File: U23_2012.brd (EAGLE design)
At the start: 150 x 100 mm, 68 parts, among them T1 BC337, X2 J1006F01P

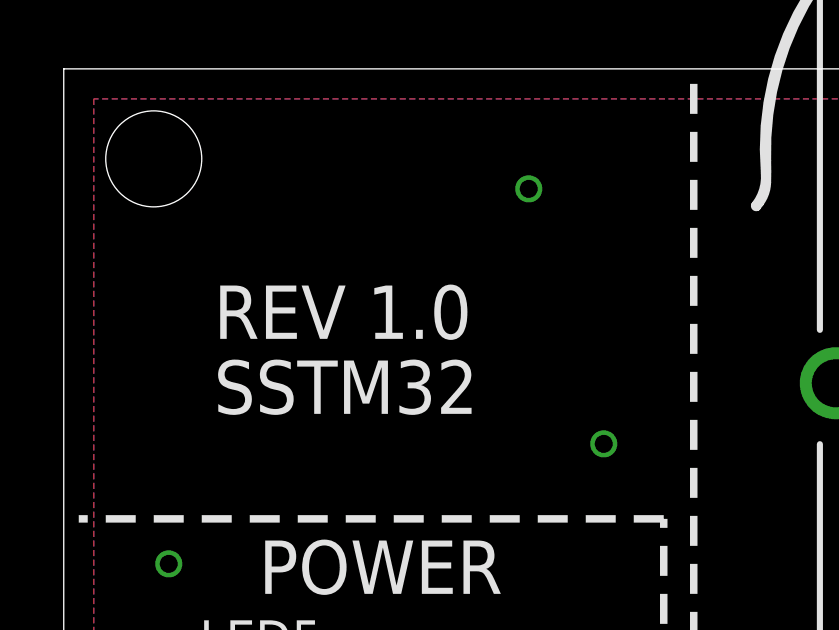
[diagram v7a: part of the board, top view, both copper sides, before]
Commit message: fixes not connected vias. rev_1.1
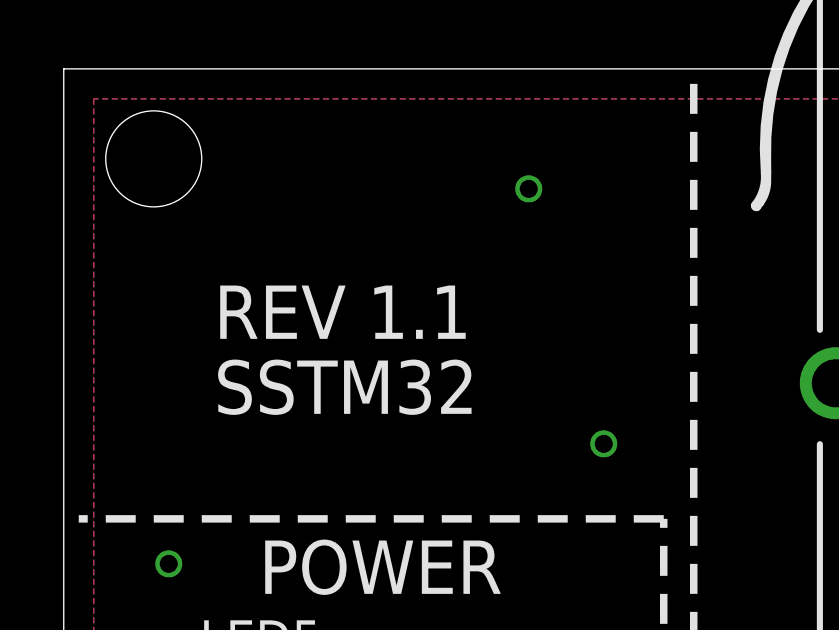
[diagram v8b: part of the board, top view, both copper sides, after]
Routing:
- net GND: vias 5 -> 45
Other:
- board text added: "REV 1.1"
- board text removed: "REV 1.0"
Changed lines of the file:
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@@
 <text x="30.5" y="20.5" size="3.81" layer="25">CHAOS COMPUTER CLUB COLOGNE</text>
 <text x="73.5" y="36.5" size="1.778" layer="25">R2R DAC</text>
-<text x="5" y="91" size="1.778" layer="25">REV 1.0</text>
+<text x="5" y="91" size="1.778" layer="25">REV 1.1</text>
 <text x="5" y="88.5" size="1.778" layer="25">SSTM32</text>
 <polygon width="0" layer="21">
@@
 <via x="6" y="40" extent="1-16" drill="0.6" shape="square"/>
 <via x="71" y="80.5" extent="1-16" drill="0.6" shape="square"/>
+<via x="15.5" y="96" extent="1-16" drill="0.6" shape="square"/>
+<via x="18" y="87.5" extent="1-16" drill="0.6" shape="square"/>
+<via x="3.5" y="83.5" extent="1-16" drill="0.6" shape="square"/>
+<via x="9" y="64" extent="1-16" drill="0.6" shape="square"/>
+<via x="9" y="56.5" extent="1-16" drill="0.6" shape="square"/>
+<via x="11" y="12.5" extent="1-16" drill="0.6" shape="square"/>
+<via x="25.5" y="16.5" extent="1-16" drill="0.6" shape="square"/>
+<via x="24" y="24" extent="1-16" drill="0.6" shape="square"/>
+<via x="31.5" y="27" extent="1-16" drill="0.6" shape="square"/>
+<via x="39.5" y="14.5" extent="1-16" drill="0.6" shape="square"/>
+<via x="49.5" y="13.5" extent="1-16" drill="0.6" shape="square"/>
+<via x="44.5" y="14.5" extent="1-16" drill="0.6" shape="square"/>
+<via x="51" y="19.5" extent="1-16" drill="0.6" shape="square"/>
+<via x="57" y="22.5" extent="1-16" drill="0.6" shape="square"/>
+<via x="31" y="31.5" extent="1-16" drill="0.6" shape="square"/>
+<via x="44.5" y="31" extent="1-16" drill="0.6" shape="square"/>
+<via x="48" y="31" extent="1-16" drill="0.6" shape="square"/>
+<via x="56.5" y="31.5" extent="1-16" drill="0.6" shape="square"/>
+<via x="56.5" y="44.5" extent="1-16" drill="0.6" shape="square"/>
+<via x="50" y="45" extent="1-16" drill="0.6" shape="square"/>
+<via x="50" y="49.5" extent="1-16" drill="0.6" shape="square"/>
+<via x="56" y="51" extent="1-16" drill="0.6" shape="square"/>
+<via x="66" y="58.5" extent="1-16" drill="0.6" shape="square"/>
+<via x="35.5" y="90" extent="1-16" drill="0.6" shape="square"/>
+<via x="71.5" y="87" extent="1-16" drill="0.6" shape="square"/>
+<via x="76.5" y="83" extent="1-16" drill="0.6" shape="square"/>
+<via x="92" y="77" extent="1-16" drill="0.6" shape="square"/>
+<via x="115.5" y="77" extent="1-16" drill="0.6" shape="square"/>
+<via x="129.5" y="77" extent="1-16" drill="0.6" shape="square"/>
+<via x="146" y="77.5" extent="1-16" drill="0.6" shape="square"/>
+<via x="118" y="58" extent="1-16" drill="0.6" shape="square"/>
+<via x="99.5" y="58" extent="1-16" drill="0.6" shape="square"/>
+<via x="97.5" y="44.5" extent="1-16" drill="0.6" shape="square"/>
+<via x="129.5" y="35" extent="1-16" drill="0.6" shape="square"/>
+<via x="123.5" y="28.5" extent="1-16" drill="0.6" shape="square"/>
+<via x="145.5" y="26.5" extent="1-16" drill="0.6" shape="square"/>
+<via x="146" y="11" extent="1-16" drill="0.6" shape="square"/>
+<via x="123" y="3.5" extent="1-16" drill="0.6" shape="square"/>
+<via x="86" y="5.5" extent="1-16" drill="0.6" shape="square"/>
+<via x="71.5" y="3.5" extent="1-16" drill="0.6" shape="square"/>
+<wire x1="64.5" y1="3" x2="71.5" y2="3.5" width="0" layer="19" extent="1-1"/>
 </signal>
 <signal name="PE15">
@@
 </polygon>
 </signal>
-<signal name="N$22">
-<via x="92" y="77" extent="1-16" drill="0.6" shape="square"/>
-</signal>
-<signal name="N$25">
-<via x="115.5" y="77" extent="1-16" drill="0.6" shape="square"/>
-</signal>
-<signal name="N$26">
-<via x="129.5" y="77" extent="1-16" drill="0.6" shape="square"/>
-</signal>
-<signal name="N$27">
-<via x="146" y="77.5" extent="1-16" drill="0.6" shape="square"/>
-</signal>
-<signal name="N$28">
-<via x="146" y="11" extent="1-16" drill="0.6" shape="square"/>
-</signal>
-<signal name="N$29">
-<via x="145.5" y="26.5" extent="1-16" drill="0.6" shape="square"/>
-</signal>
-<signal name="N$30">
-<via x="129.5" y="35" extent="1-16" drill="0.6" shape="square"/>
-</signal>
-<signal name="N$31">
-<via x="123.5" y="28.5" extent="1-16" drill="0.6" shape="square"/>
-</signal>
-<signal name="N$32">
-<via x="97.5" y="44.5" extent="1-16" drill="0.6" shape="square"/>
-</signal>
-<signal name="N$33">
-<via x="66" y="58.5" extent="1-16" drill="0.6" shape="square"/>
-</signal>
-<signal name="N$34">
-<via x="99.5" y="58" extent="1-16" drill="0.6" shape="square"/>
-</signal>
-<signal name="N$35">
-<via x="118" y="58" extent="1-16" drill="0.6" shape="square"/>
-</signal>
-<signal name="N$36">
-<via x="56" y="51" extent="1-16" drill="0.6" shape="square"/>
-</signal>
-<signal name="N$37">
-<via x="50" y="49.5" extent="1-16" drill="0.6" shape="square"/>
-</signal>
-<signal name="N$38">
-<via x="50" y="45" extent="1-16" drill="0.6" shape="square"/>
-</signal>
-<signal name="N$39">
-<via x="56.5" y="44.5" extent="1-16" drill="0.6" shape="square"/>
-</signal>
-<signal name="N$40">
-<via x="56.5" y="31.5" extent="1-16" drill="0.6" shape="square"/>
-</signal>
-<signal name="N$41">
-<via x="48" y="31" extent="1-16" drill="0.6" shape="square"/>
-</signal>
-<signal name="N$42">
-<via x="44.5" y="31" extent="1-16" drill="0.6" shape="square"/>
-</signal>
-<signal name="N$43">
-<via x="51" y="19.5" extent="1-16" drill="0.6" shape="square"/>
-</signal>
-<signal name="N$44">
-<via x="57" y="22.5" extent="1-16" drill="0.6" shape="square"/>
-</signal>
-<signal name="N$45">
-<via x="49.5" y="13.5" extent="1-16" drill="0.6" shape="square"/>
-</signal>
-<signal name="N$46">
-<via x="44.5" y="14.5" extent="1-16" drill="0.6" shape="square"/>
-</signal>
-<signal name="N$47">
-<via x="39.5" y="14.5" extent="1-16" drill="0.6" shape="square"/>
-</signal>
-<signal name="N$48">
-<via x="25.5" y="16.5" extent="1-16" drill="0.6" shape="square"/>
-</signal>
-<signal name="N$49">
-<via x="24" y="24" extent="1-16" drill="0.6" shape="square"/>
-</signal>
-<signal name="N$50">
-<via x="31" y="31.5" extent="1-16" drill="0.6" shape="square"/>
-</signal>
-<signal name="N$51">
-<via x="31.5" y="27" extent="1-16" drill="0.6" shape="square"/>
-</signal>
-<signal name="N$52">
-<via x="11" y="12.5" extent="1-16" drill="0.6" shape="square"/>
-</signal>
-<signal name="N$53">
-<via x="9" y="56.5" extent="1-16" drill="0.6" shape="square"/>
-</signal>
-<signal name="N$54">
-<via x="9" y="64" extent="1-16" drill="0.6" shape="square"/>
-</signal>
-<signal name="N$55">
-<via x="3.5" y="83.5" extent="1-16" drill="0.6" shape="square"/>
-</signal>
-<signal name="N$56">
-<via x="18" y="87.5" extent="1-16" drill="0.6" shape="square"/>
-</signal>
-<signal name="N$57">
-<via x="15.5" y="96" extent="1-16" drill="0.6" shape="square"/>
-</signal>
-<signal name="N$58">
-<via x="35.5" y="90" extent="1-16" drill="0.6" shape="square"/>
-</signal>
-<signal name="N$59">
-<via x="71.5" y="87" extent="1-16" drill="0.6" shape="square"/>
-</signal>
-<signal name="N$60">
-<via x="76.5" y="83" extent="1-16" drill="0.6" shape="square"/>
-</signal>
 <signal name="N$61">
 <via x="86" y="36.5" extent="1-16" drill="0.6" shape="square"/>
 </signal>
-<signal name="N$62">
-<via x="71.5" y="3.5" extent="1-16" drill="0.6" shape="square"/>
-</signal>
-<signal name="N$63">
-<via x="86" y="5.5" extent="1-16" drill="0.6" shape="square"/>
-</signal>
-<signal name="N$64">
-<via x="123" y="3.5" extent="1-16" drill="0.6" shape="square"/>
-</signal>
 </signals>
